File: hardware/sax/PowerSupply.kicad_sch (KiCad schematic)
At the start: 8 parts, among them U1201 TPSM365R6FRDNR

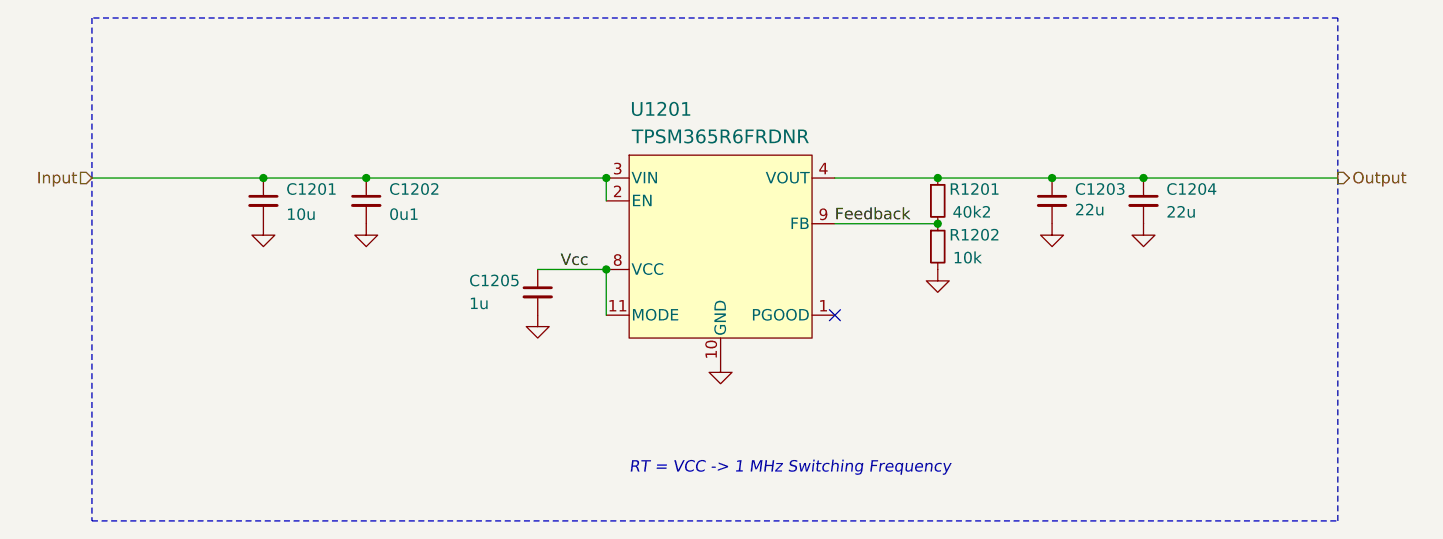
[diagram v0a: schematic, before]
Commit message: Replace step-down
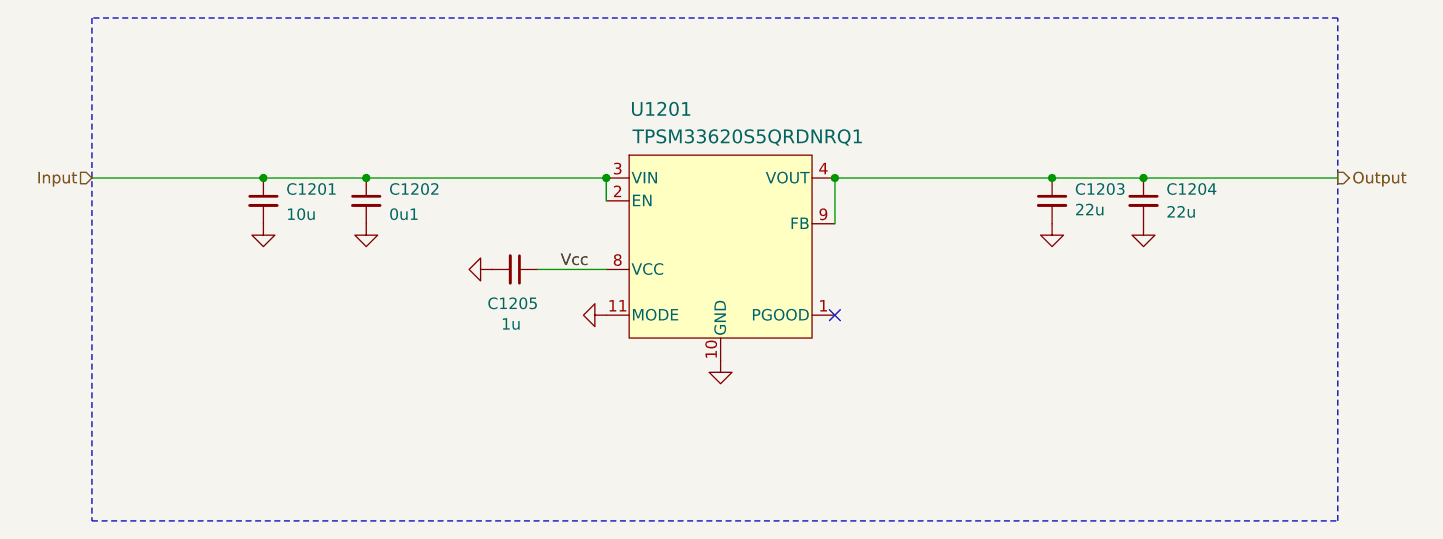
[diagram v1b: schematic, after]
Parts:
- removed R1201: 40k2, V2_Resistor_SMD:R_0603, symbol V2_Resistor:0603_40k2
- removed R1202: 10k, V2_Resistor_SMD:R_0603, symbol V2_Resistor:0603_10k
- U1201: value TPSM365R6FRDNR -> TPSM33620S5QRDNRQ1; symbol V2_Converter_DCDC:TPSM365R6FRDNR -> V2_Converter_DCDC:TPSM33620S5QRDNRQ1; Mouser 595-TPSM365R6FRDNR -> 595-SM33620S5QRDNRQ1; Product TPSM365R6FRDNR -> TPSM33620S5QRDNRQ1; Rating 600mA -> 2A
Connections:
- net Feedback is gone; now on net Output: U1201.9 (FB)
- net GND: now also U1201.11 (MODE)
- net Vcc: no longer U1201.11 (MODE)
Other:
- note removed: "RT = VCC -> 1 MHz Switching Frequency"
- title: Power Supply -> V2 sax
- moved on the sheet: C1205

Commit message: Limit up note length to 3 seconds
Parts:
- C1201, C1202, C1203, C1204, C1205: Id (none) -> Capacitor:${SYMBOL_NAME}
- U1201: Id (none) -> DCDC:${SYMBOL_NAME}
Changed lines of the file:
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@@
+			)
+		)
+		(property "Id" "DCDC:${SYMBOL_NAME}"
+			(at 148.59 147.32 0)
+			(hide yes)
+			(show_name no)
+			(do_not_autoplace no)
+			(effects
+				(font
+					(size 1.27 1.27)
+				)
+			)
+		)
+		(property "Sim.Enable" ""
+			(at 148.59 102.87 0)
+			(hide yes)
+			(show_name no)
+			(do_not_autoplace no)
+			(effects
+				(font
+					(size 1.27 1.27)
+				)
+			)
+		)
+		(property "Voltage" ""
+			(at 148.59 102.87 0)
+			(hide yes)
+			(show_name no)
+			(do_not_autoplace no)
+			(effects
+				(font
+					(size 1.27 1.27)
+				)
 			)
 		)
@@
 			)
 		)
+		(property "Id" "Capacitor:${SYMBOL_NAME}"
+			(at 109.22 113.03 0)
+			(hide yes)
+			(show_name no)
+			(do_not_autoplace no)
+			(effects
+				(font
+					(size 1.27 1.27)
+				)
+			)
+		)
+		(property "Sim.Enable" ""
+			(at 109.22 97.79 0)
+			(hide yes)
+			(show_name no)
+			(do_not_autoplace no)
+			(effects
+				(font
+					(size 1.27 1.27)
+				)
+			)
+		)
+		(property "Voltage" ""
+			(at 109.22 97.79 0)
+			(hide yes)
+			(show_name no)
+			(do_not_autoplace no)
+			(effects
+				(font
+					(size 1.27 1.27)
+				)
+			)
+		)
 		(pin "1"
 		)
@@
 			)
 		)
+		(property "Id" "Capacitor:${SYMBOL_NAME}"
+			(at 195.58 113.03 0)
+			(hide yes)
+			(show_name no)
+			(do_not_autoplace no)
+			(effects
+				(font
+					(size 1.27 1.27)
+				)
+			)
+		)
+		(property "Sim.Enable" ""
+			(at 195.58 97.79 0)
+			(hide yes)
+			(show_name no)
+			(do_not_autoplace no)
+			(effects
+				(font
+					(size 1.27 1.27)
+				)
+			)
+		)
+		(property "Voltage" ""
+			(at 195.58 97.79 0)
+			(hide yes)
+			(show_name no)
+			(do_not_autoplace no)
+			(effects
+				(font
+					(size 1.27 1.27)
+				)
+			)
+		)
 		(pin "1"
 		)
@@
 			)
 		)
+		(property "Id" "Capacitor:${SYMBOL_NAME}"
+			(at 110.49 105.41 0)
+			(hide yes)
+			(show_name no)
+			(do_not_autoplace no)
+			(effects
+				(font
+					(size 1.27 1.27)
+				)
+			)
+		)
+		(property "Sim.Enable" ""
+			(at 125.73 105.41 90)
+			(hide yes)
+			(show_name no)
+			(do_not_autoplace no)
+			(effects
+				(font
+					(size 1.27 1.27)
+				)
+			)
+		)
+		(property "Voltage" ""
+			(at 125.73 105.41 90)
+			(hide yes)
+			(show_name no)
+			(do_not_autoplace no)
+			(effects
+				(font
+					(size 1.27 1.27)
+				)
+			)
+		)
 		(pin "1"
 		)
@@
 			)
 		)
+		(property "Id" "Capacitor:${SYMBOL_NAME}"
+			(at 185.42 113.03 0)
+			(hide yes)
+			(show_name no)
+			(do_not_autoplace no)
+			(effects
+				(font
+					(size 1.27 1.27)
+				)
+			)
+		)
+		(property "Sim.Enable" ""
+			(at 185.42 97.79 0)
+			(hide yes)
+			(show_name no)
+			(do_not_autoplace no)
+			(effects
+				(font
+					(size 1.27 1.27)
+				)
+			)
+		)
+		(property "Voltage" ""
+			(at 185.42 97.79 0)
+			(hide yes)
+			(show_name no)
+			(do_not_autoplace no)
+			(effects
+				(font
+					(size 1.27 1.27)
+				)
+			)
+		)
 		(pin "1"
 		)
@@
 			(hide yes)
 			(show_name no)
+			(do_not_autoplace no)
+			(effects
+				(font
+					(size 1.27 1.27)
+				)
+			)
+		)
+		(property "Id" "Capacitor:${SYMBOL_NAME}"
+			(at 97.79 113.03 0)
+			(hide yes)
+			(show_name no)
+			(do_not_autoplace no)
+			(effects
+				(font
+					(size 1.27 1.27)
+				)
+			)
+		)
+		(property "Sim.Enable" ""
+			(at 97.79 97.79 0)
+			(hide yes)
+			(show_name no)
+			(do_not_autoplace no)
+			(effects
+				(font
+					(size 1.27 1.27)
+				)
+			)
+		)
+		(property "Voltage" ""
+			(at 97.79 97.79 0)
+			(hide yes)
+			(show_name no)
